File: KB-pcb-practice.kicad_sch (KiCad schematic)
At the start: 56 parts, among them J1 Conn_01x03, SW1 Reset, SW2 Boot, U1 RP2040, U2 IS31FL3742A-QFLS4-TR, U3 W25Q128JVS, U4 IS31FL3742A-QFLS4-TR, U5 NCP1117-3.3_SOT223, Y1 ABLS-12.000MHZ-B4-T

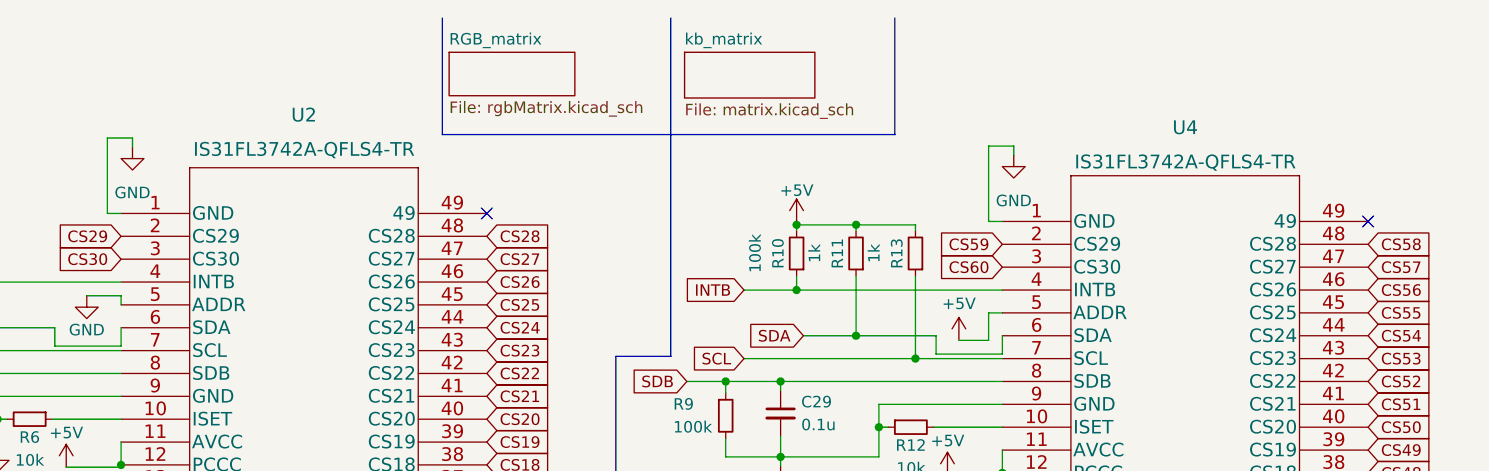
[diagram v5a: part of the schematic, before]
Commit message: Fixed Majority of Errors in ERC
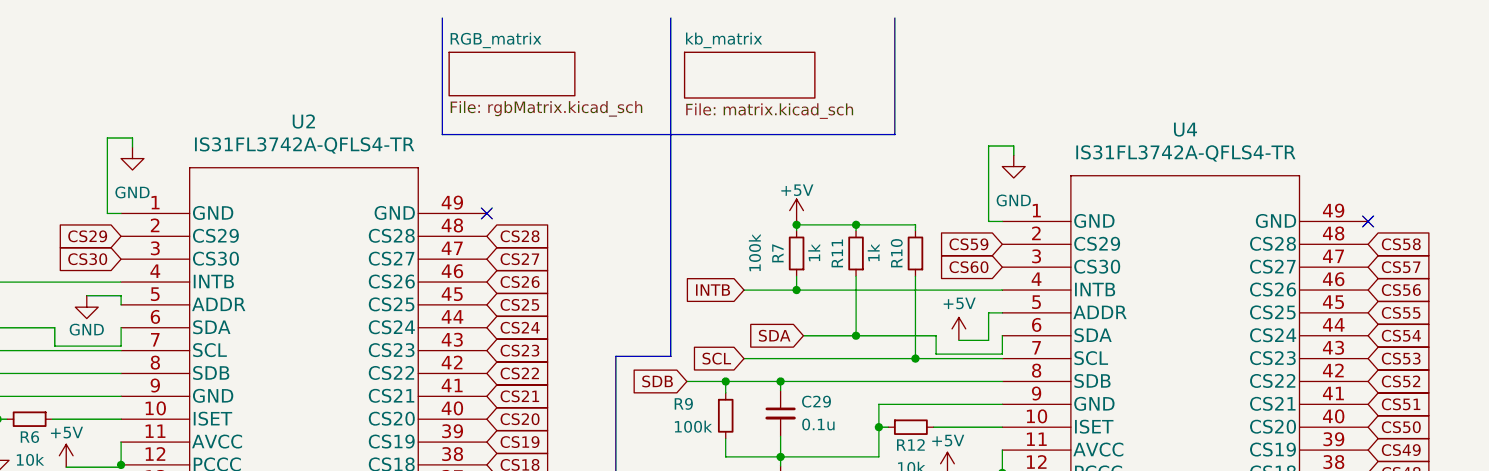
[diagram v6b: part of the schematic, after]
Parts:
- U2, U4: symbol ul_IS31FL3742A-QFLS4-TR:IS31FL3742A-QFLS4-TR -> ul_IS31FL3742A-QFLS4-TR_custom:IS31FL3742A-QFLS4-TR
- renumbered R13 to R10, R10 to R7
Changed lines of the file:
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@@
     )
   )
-  (symbol (lib_id "ul_IS31FL3742A-QFLS4-TR:IS31FL3742A-QFLS4-TR") (at 131.445 33.655 0) (unit 1)
-    (in_bom yes) (on_board yes) (dnp no) (fields_autoplaced)
-    (property "Reference" "U2" (at 151.765 22.733 0)
+  (symbol (lib_id "ul_IS31FL3742A-QFLS4-TR_custom:IS31FL3742A-QFLS4-TR") (at 131.445 33.655 0) (unit 1)
+    (in_bom yes) (on_board yes) (dnp no) (fields_autoplaced)
+    (property "Reference" "U2" (at 151.765 23.495 0)
       (effects (font (size 1.524 1.524)))
     )
-    (property "Value" "IS31FL3742A-QFLS4-TR" (at 151.765 26.543 0)
+    (property "Value" "IS31FL3742A-QFLS4-TR" (at 151.765 26.035 0)
       (effects (font (size 1.524 1.524)))
     )
@@
   (symbol (lib_id "Device:R_Small") (at 206.502 38.1 180) (unit 1)
     (in_bom yes) (on_board yes) (dnp no)
-    (property "Reference" "R10" (at 204.47 38.1 90)
+    (property "Reference" "R7" (at 204.47 38.1 90)
       (effects (font (size 1.27 1.27)))
     )
@@
       (project "KB-pcb-practice"
         (path "/806fdcd7-25b2-4878-addb-1faa319c0ab0"
-          (reference "R10") (unit 1)
+          (reference "R7") (unit 1)
         )
       )
@@
   (symbol (lib_id "Device:R_Small") (at 219.71 38.1 180) (unit 1)
     (in_bom yes) (on_board yes) (dnp no)
-    (property "Reference" "R13" (at 217.678 38.1 90)
+    (property "Reference" "R10" (at 217.678 38.1 90)
       (effects (font (size 1.27 1.27)))
     )
@@
       (project "KB-pcb-practice"
         (path "/806fdcd7-25b2-4878-addb-1faa319c0ab0"
-          (reference "R13") (unit 1)
+          (reference "R10") (unit 1)
         )
       )
@@
     )
   )
-  (symbol (lib_id "ul_IS31FL3742A-QFLS4-TR:IS31FL3742A-QFLS4-TR") (at 229.362 34.544 0) (unit 1)
-    (in_bom yes) (on_board yes) (dnp no) (fields_autoplaced)
-    (property "Reference" "U4" (at 249.682 24.13 0)
+  (symbol (lib_id "ul_IS31FL3742A-QFLS4-TR_custom:IS31FL3742A-QFLS4-TR") (at 229.362 34.544 0) (unit 1)
+    (in_bom yes) (on_board yes) (dnp no) (fields_autoplaced)
+    (property "Reference" "U4" (at 249.682 24.384 0)
       (effects (font (size 1.524 1.524)))
     )
-    (property "Value" "IS31FL3742A-QFLS4-TR" (at 249.682 27.94 0)
+    (property "Value" "IS31FL3742A-QFLS4-TR" (at 249.682 26.924 0)
       (effects (font (size 1.524 1.524)))
     )

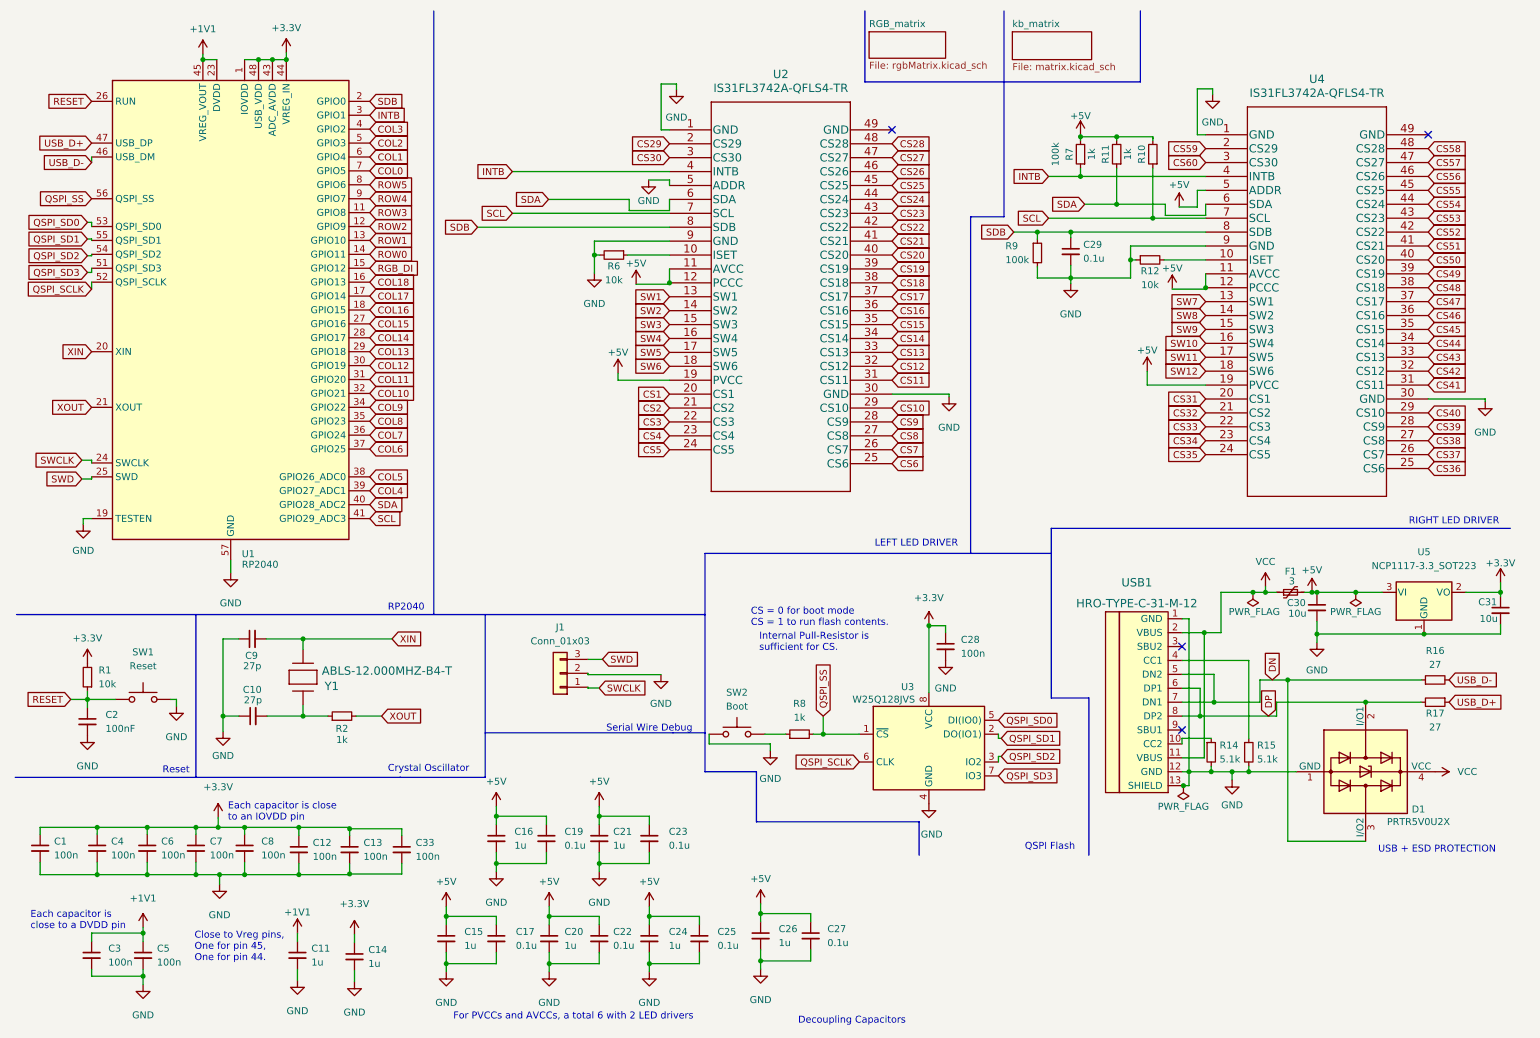
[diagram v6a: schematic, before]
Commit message: Added RGB Underglow
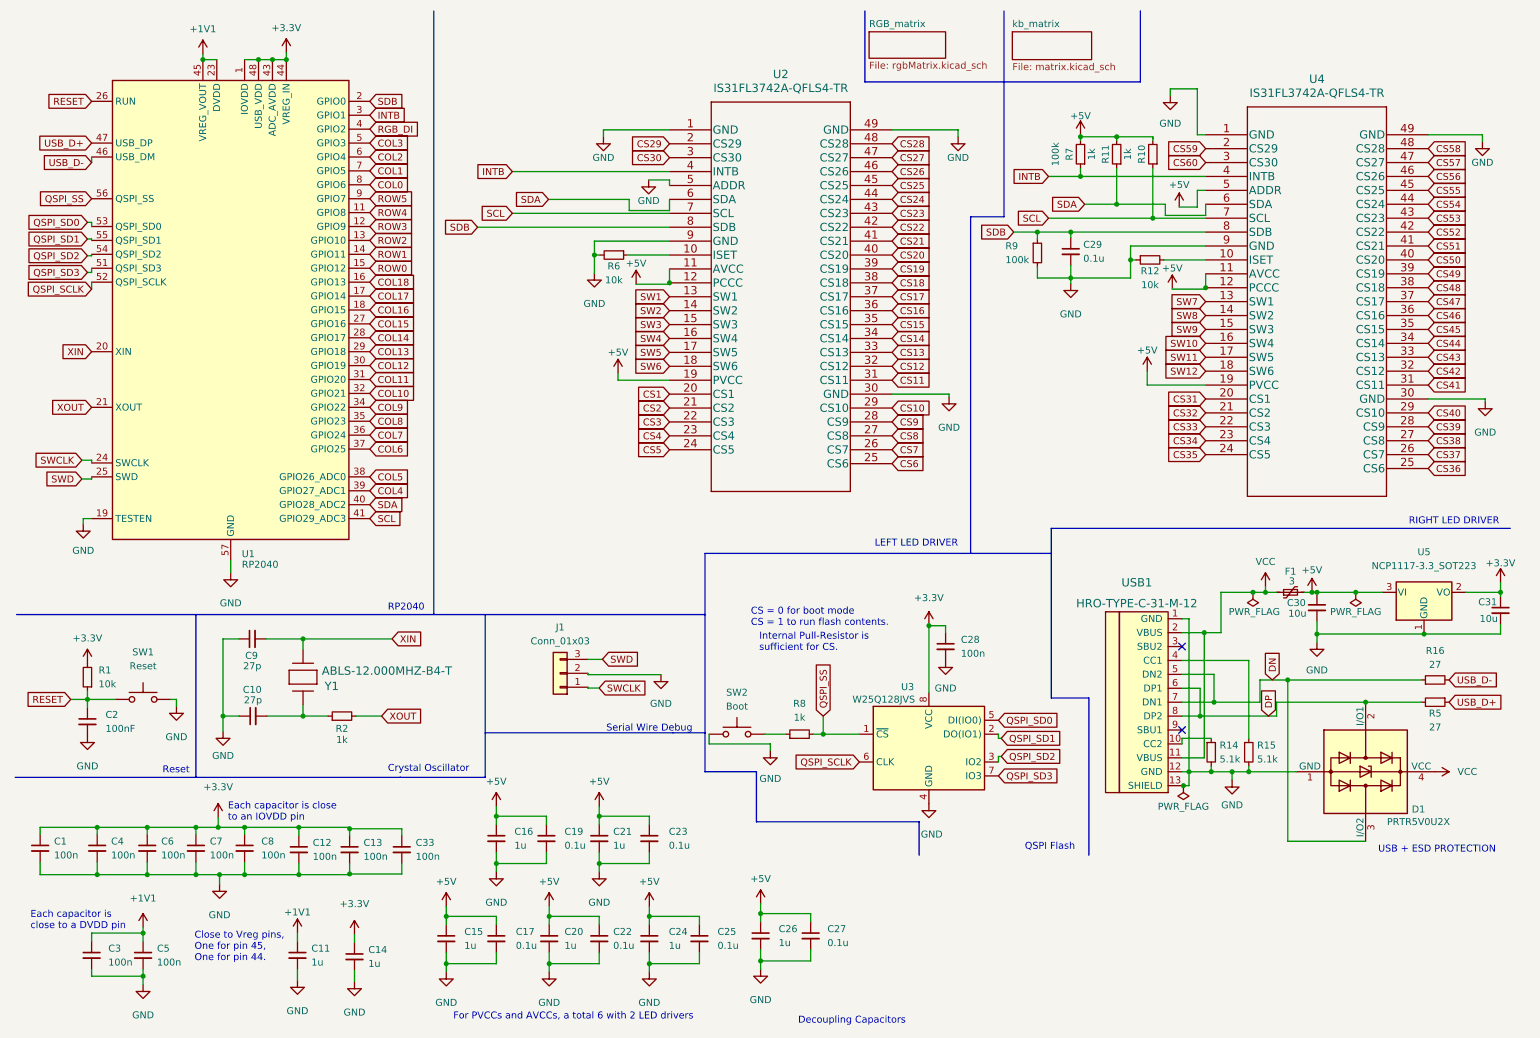
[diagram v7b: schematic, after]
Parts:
- renumbered R17 to R5
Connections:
- net COL0: now also U1.8 (GPIO6); no longer U1.7 (GPIO5)
- net COL1: now also U1.7 (GPIO5); no longer U1.6 (GPIO4)
- net COL2: now also U1.6 (GPIO4); no longer U1.5 (GPIO3)
- net COL3: now also U1.5 (GPIO3); no longer U1.4 (GPIO2)
- net GND: now also U2.49 (GND), U4.49 (GND)
- net RGB_DI: now also U1.4 (GPIO2); no longer U1.15 (GPIO12)
- net ROW0: now also U1.15 (GPIO12); no longer U1.14 (GPIO11)
- net ROW1: now also U1.14 (GPIO11); no longer U1.13 (GPIO10)
- net ROW2: now also U1.13 (GPIO10); no longer U1.12 (GPIO9)
- net ROW3: now also U1.12 (GPIO9); no longer U1.11 (GPIO8)
- net ROW4: now also U1.11 (GPIO8); no longer U1.9 (GPIO7)
- net ROW5: now also U1.9 (GPIO7); no longer U1.8 (GPIO6)
- no-connect marks 4 -> 2
